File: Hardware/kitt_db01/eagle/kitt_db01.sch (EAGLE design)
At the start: 24 parts, among them Q1 [MMBF170], U1 ADNS-3080, U2 MIC5205-3.3YM5TR, X1 RESON

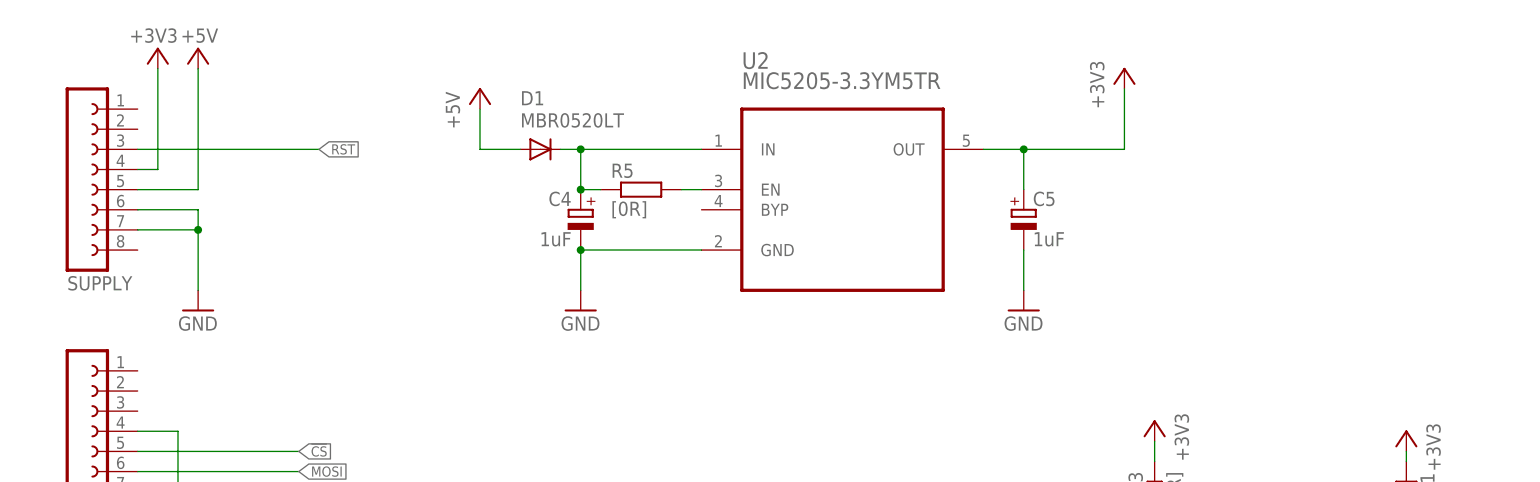
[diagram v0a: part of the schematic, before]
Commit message: board snapshot of db01 + added patching area for north-west port
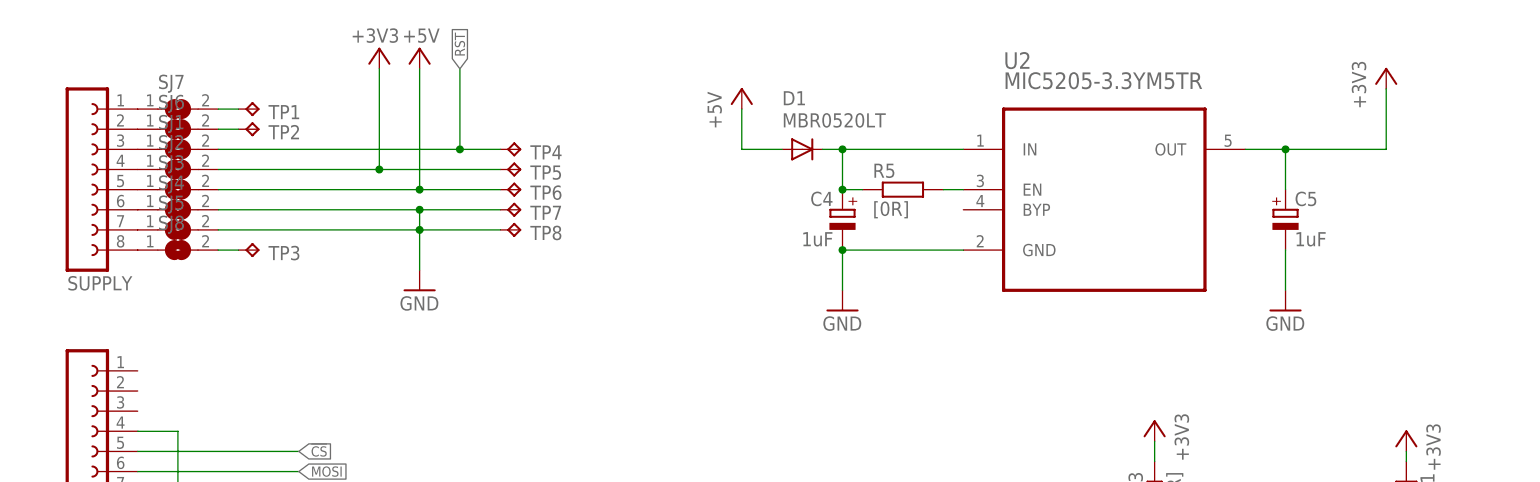
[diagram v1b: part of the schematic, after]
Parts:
- added SJ1, SJ2, SJ3, SJ4, SJ5, SJ6, SJ7, SJ8: (no value), jumper:SJ
- added TP1, TP2, TP3, TP4, TP5, TP6, TP7, TP8: TPPAD1-13, testpad:TPPAD1-13
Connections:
- new net N$12: SJ1.1, SUPPLY.3
- new net N$13: SJ2.1, SUPPLY.4
- new net N$134: SJ3.1, SUPPLY.5
- new net N$135: SJ4.1, SUPPLY.6
- new net N$136: SJ5.1, SUPPLY.7
- new net N$137: SJ7.1, SUPPLY.1
- new net N$138: SJ6.1, SUPPLY.2
- new net N$139: SJ8.1, SUPPLY.8
- new net N$140: SJ7.2, TP1.TP
- new net N$141: SJ6.2, TP2.TP
- new net N$142: SJ8.2, TP3.TP
- net +3V3: now also SJ2.2, TP5.TP; no longer SUPPLY.4
- net +5V: now also SJ3.2, TP6.TP; no longer SUPPLY.5
- net GND: now also SJ4.2, SJ5.2, TP7.TP, TP8.TP; no longer SUPPLY.6, SUPPLY.7
- net RST: now also SJ1.2, TP4.TP; no longer SUPPLY.3
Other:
- moved on the sheet: C4, C5, D1, R5, U2

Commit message: snapshot of board db01 + added southwest patching area
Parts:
- added SJ10, SJ11, SJ12, SJ13, SJ14, SJ15, SJ16, SJ17, SJ18, SJ19, SJ9: (no value), jumper:SJ
- added TP10, TP11, TP12, TP13, TP14, TP15, TP16, TP17, TP18, TP9: TPPAD1-13, testpad:TPPAD1-13
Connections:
- new net N$143: SJ9.1, SV1.1
- new net N$144: SJ10.1, SV1.2
- new net N$145: SJ11.1, SV1.3
- new net N$146: SJ11.2, TP9.TP
- new net N$147: SJ12.1, SV1.4
- new net N$148: SJ13.1, SV1.5
- new net N$149: SJ14.1, SV1.6
- new net N$150: SJ15.1, SV1.7
- new net N$151: SJ16.1, SV1.8
- new net N$152: SJ17.1, SV1.9
- new net N$153: SJ18.1, SV1.10
- new net SCL: SJ9.2, TP11.TP
- new net SDA: SJ10.2, TP10.TP
- net !CS: now also SJ13.2, TP12.TP; no longer SV1.5
- net !LEDCTRL: now also SJ18.2, TP17.TP; no longer SV1.10
- net !PD: now also SJ17.2, TP16.TP; no longer SV1.9
- net GND: now also SJ12.2, TP18.TP; no longer SV1.4
- net MISO: now also SJ15.2, TP14.TP; no longer SV1.7
- net MOSI: now also SJ14.2, TP13.TP; no longer SV1.6
- net SCLK: now also SJ16.2, TP15.TP; no longer SV1.8
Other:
- moved on the sheet: C1, C2, C3, LED1, Q1, R1, R2, R3, R7, U1, X1

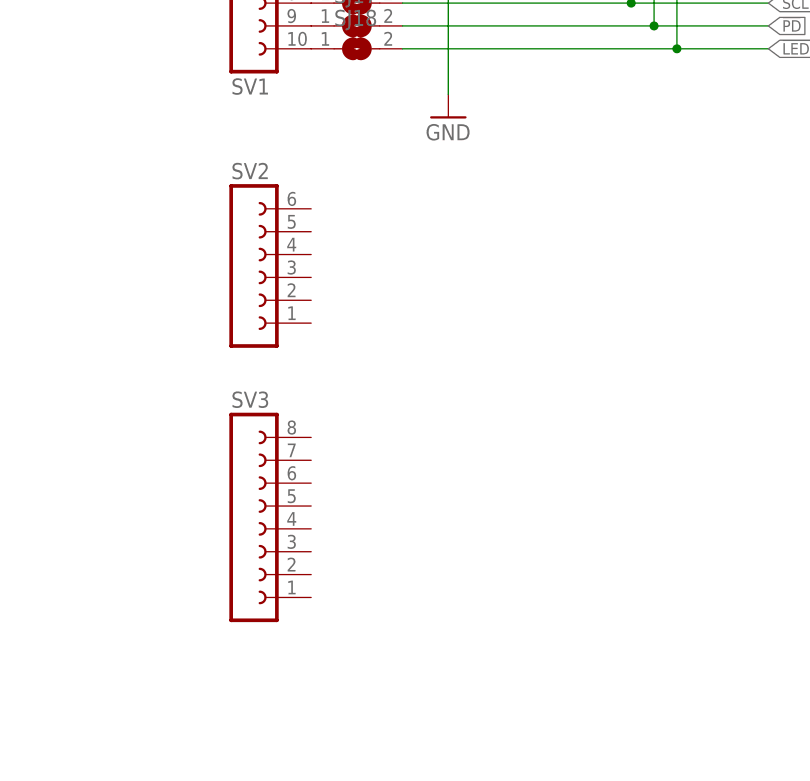
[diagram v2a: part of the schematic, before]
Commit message: snapshot of db01 board -> added northeast and southeast patchthough to pins
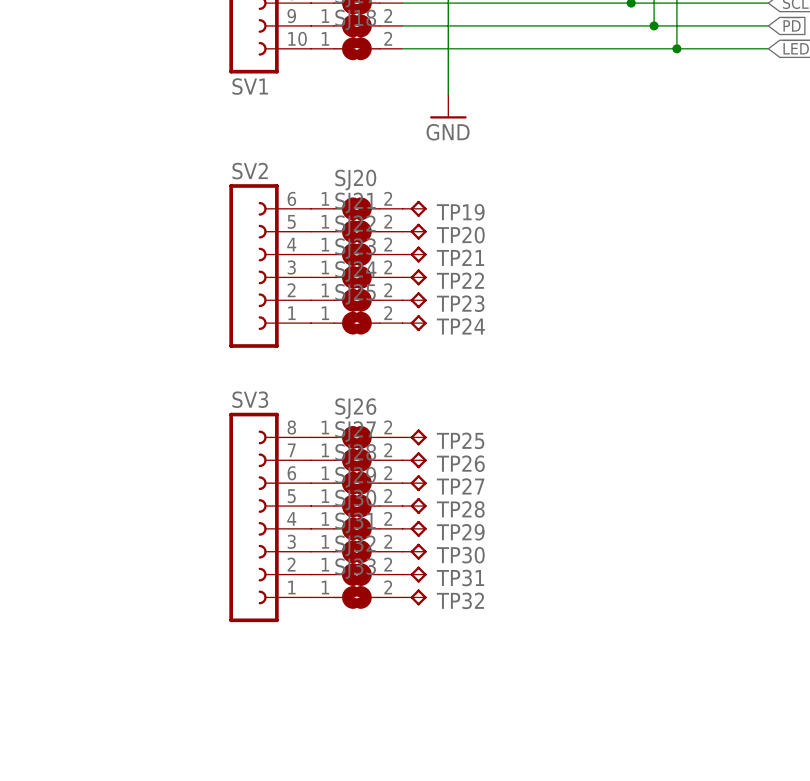
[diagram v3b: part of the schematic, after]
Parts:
- added SJ20, SJ21, SJ22, SJ23, SJ24, SJ25, SJ26, SJ27, SJ28, SJ29, SJ30, SJ31, SJ32, SJ33: (no value), jumper:SJ
- added TP19, TP20, TP21, TP22, TP23, TP24, TP25, TP26, TP27, TP28, TP29, TP30, TP31, TP32: TPPAD1-13, testpad:TPPAD1-13
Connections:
- new net N$154: SJ20.1, SV2.6
- new net N$155: SJ21.1, SV2.5
- new net N$156: SJ22.1, SV2.4
- new net N$157: SJ23.1, SV2.3
- new net N$158: SJ24.1, SV2.2
- new net N$159: SJ25.1, SV2.1
- new net N$160: SJ26.1, SV3.8
- new net N$161: SJ27.1, SV3.7
- new net N$162: SJ28.1, SV3.6
- new net N$163: SJ29.1, SV3.5
- new net N$164: SJ30.1, SV3.4
- new net N$165: SJ31.1, SV3.3
- new net N$166: SJ32.1, SV3.2
- new net N$167: SJ33.1, SV3.1
- new net N$168: SJ20.2, TP19.TP
- new net N$169: SJ21.2, TP20.TP
- new net N$170: SJ22.2, TP21.TP
- new net N$171: SJ23.2, TP22.TP
- new net N$172: SJ24.2, TP23.TP
- new net N$173: SJ25.2, TP24.TP
- new net N$174: SJ26.2, TP25.TP
- new net N$175: SJ27.2, TP26.TP
- new net N$176: SJ28.2, TP27.TP
- new net N$177: SJ29.2, TP28.TP
- new net N$178: SJ30.2, TP29.TP
- new net N$179: SJ31.2, TP30.TP
- new net N$180: SJ32.2, TP31.TP
- new net N$181: SJ33.2, TP32.TP

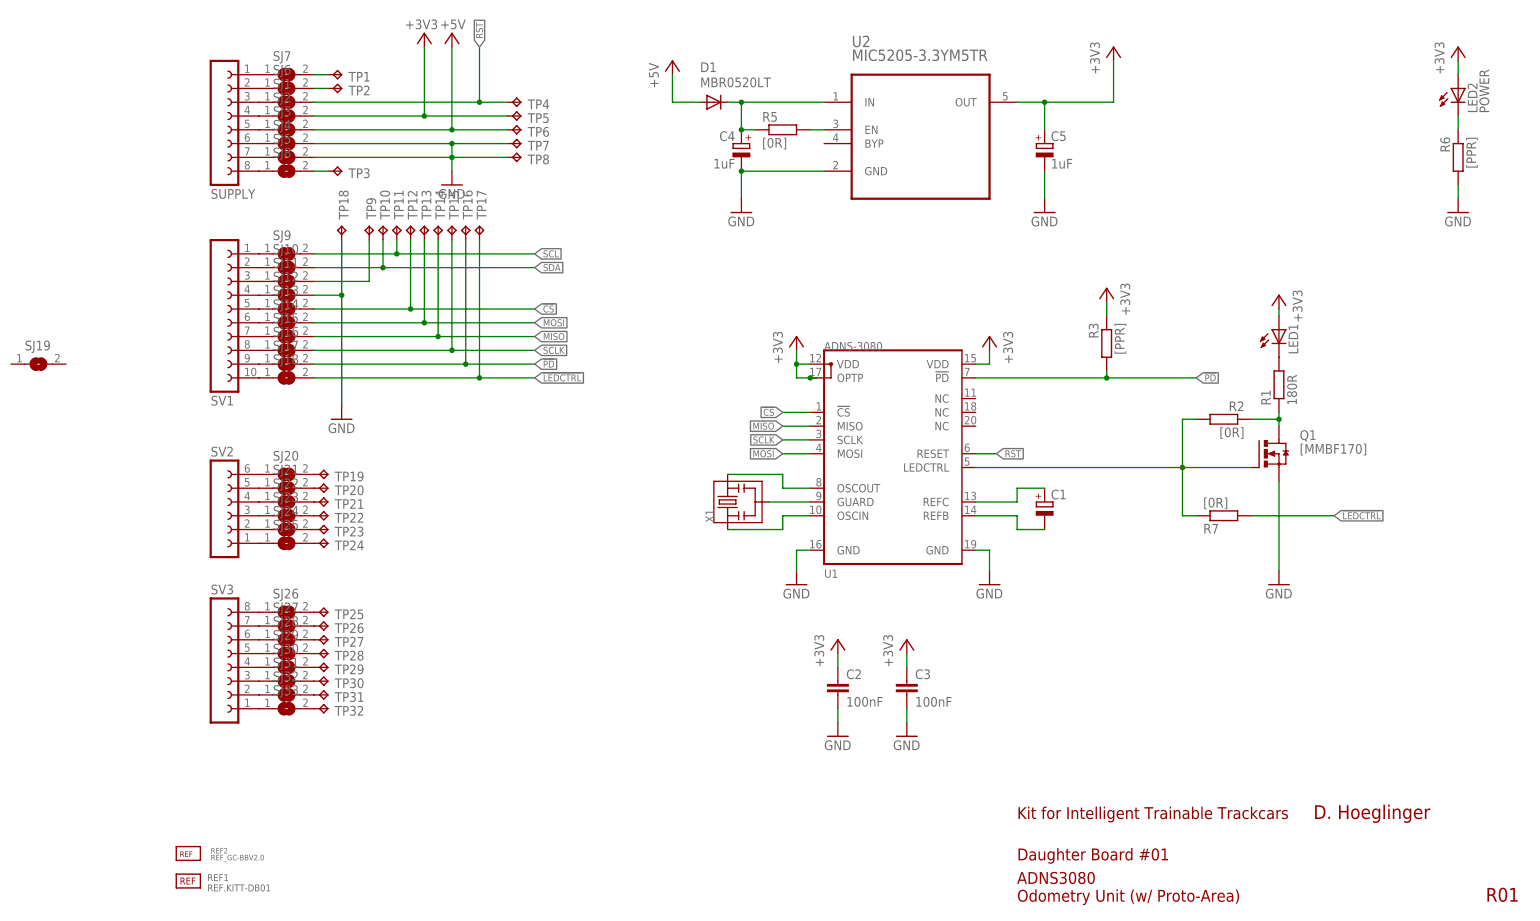
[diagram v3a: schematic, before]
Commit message: snapshot of db01 board layout -> added alternate LEDs for illuminating surface
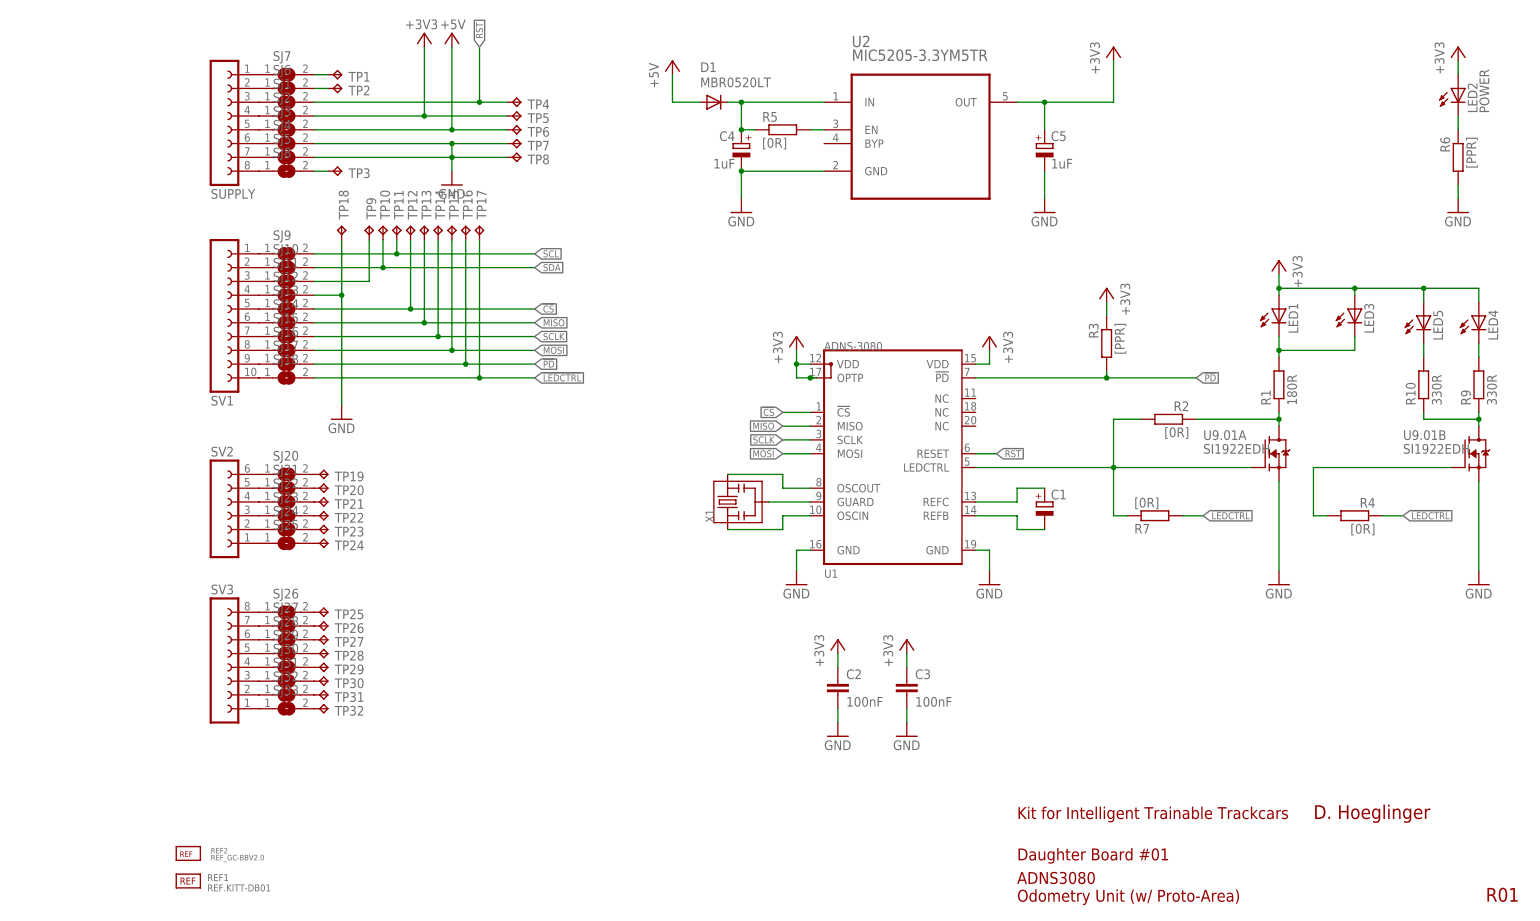
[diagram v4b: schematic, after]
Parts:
- removed Q1: [MMBF170], transistor-power:N-HEXFET-2D_SOT232-
- removed SJ19: (no value), jumper:SJ
- added LED3, LED4, LED5: (no value), led:LEDCHIP-LED0805
- added R10, R9: 330R, rcl:R-EU_R0805
- added R4: [0R], rcl:R-EU_R0805
- added U9.01: SI1922EDH, kitt.ic:SI1922EDH
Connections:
- new net N$184: R4.2, U9.01B.G
- new net N$185: LED4.C, R9.2
- new net N$186: R10.1, R9.1, U9.01B.D
- new net N$187: LED5.C, R10.2
- net !LEDCTRL: now also R4.1
- net +3V3: now also LED3.A, LED4.A, LED5.A
- net GND: now also U9.01A.S, U9.01B.S; no longer Q1.S
- net MISO: now also SJ14.2, TP13.TP; no longer SJ15.2, TP14.TP
- net MOSI: now also SJ16.2, TP15.TP; no longer SJ14.2, TP13.TP
- net N$4: now also U9.01A.G; no longer Q1.G
- net N$7: now also U9.01A.D; no longer Q1.D
- net N$8: now also LED3.C
- net SCLK: now also SJ15.2, TP14.TP; no longer SJ16.2, TP15.TP
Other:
- moved on the sheet: LED1, R2, R7
